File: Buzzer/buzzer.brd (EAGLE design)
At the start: 100 x 80 mm, 27 parts

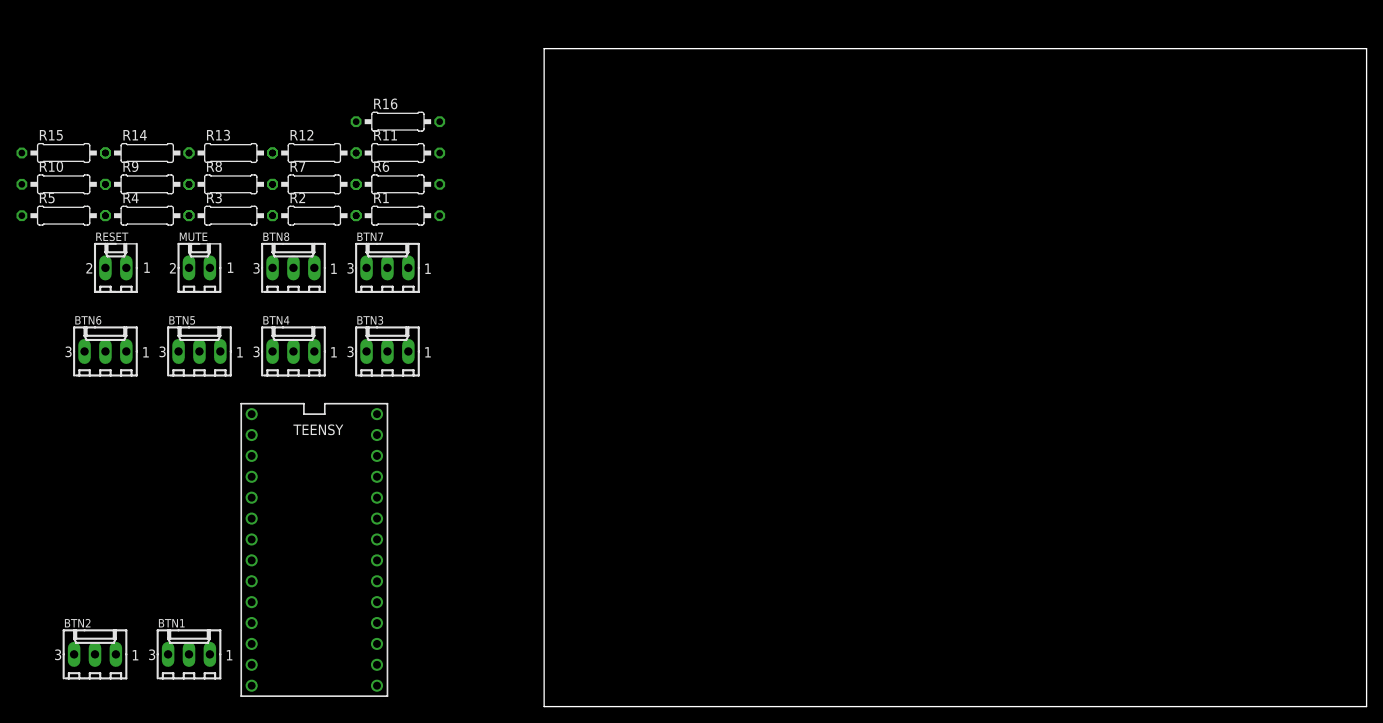
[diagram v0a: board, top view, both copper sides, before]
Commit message: Work on Eagle board design Unfinished, but it'll do as veroboard is a mess anyway
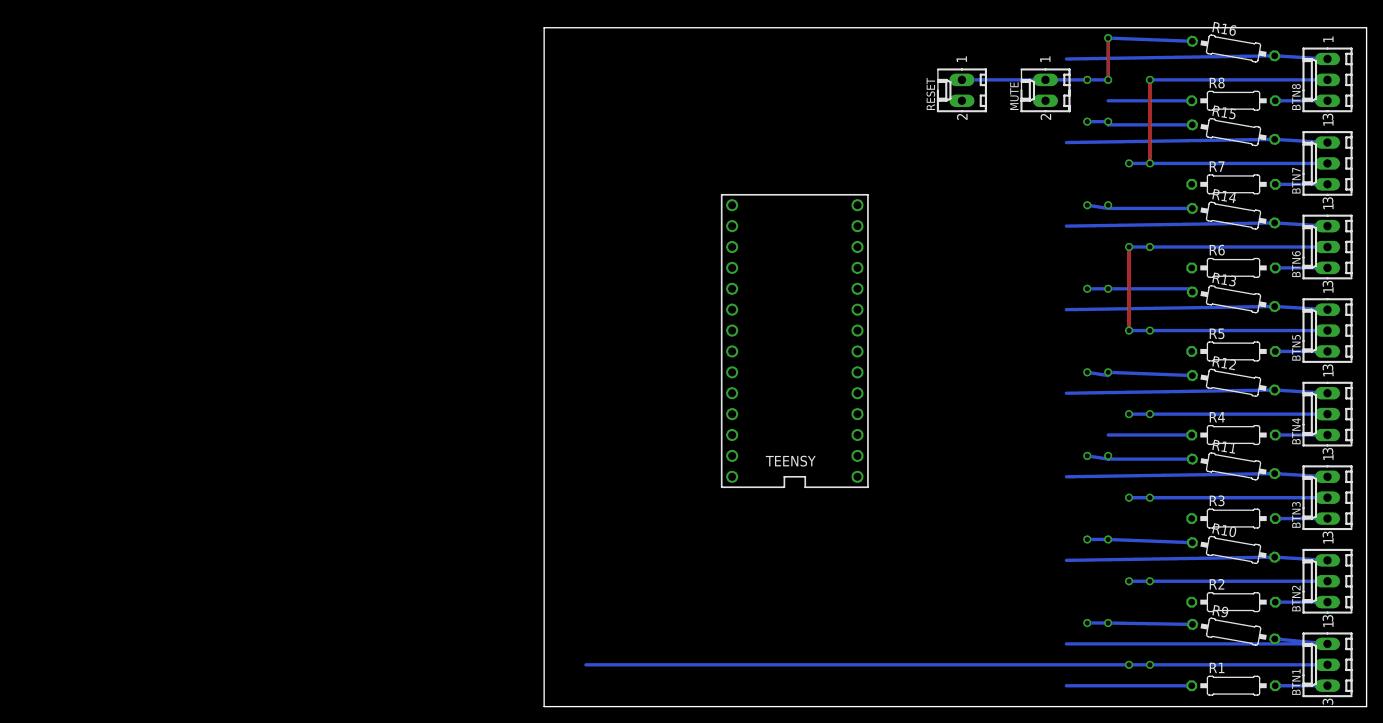
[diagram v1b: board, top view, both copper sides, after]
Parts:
- moved BTN2 150.1 mm to (95.2, 15.2), turned to 90 degrees
- moved BTN6 149.1 mm to (95.2, 55.9), turned to 90 degrees
- moved R10 149.0 mm to (83.8, 19.1), turned to 350 degrees
- moved R5 143.2 mm to (83.8, 43.2)
- moved R9 142.9 mm to (83.8, 9.11), turned to 350 degrees
- moved R15 142.3 mm to (83.8, 69.8), turned to 350 degrees
- moved BTN1 138.4 mm to (95.2, 5.08), turned to 90 degrees
- moved BTN5 137.2 mm to (95.2, 45.7), turned to 90 degrees
- moved R4 134.7 mm to (83.8, 33.0)
- moved R14 132.3 mm to (83.8, 59.7), turned to 350 degrees
- moved BTN8 127.8 mm to (95.2, 76.2), turned to 90 degrees
- moved R3 127.4 mm to (83.8, 22.9)
- moved BTN4 126.0 mm to (95.2, 35.6), turned to 90 degrees
- moved R13 123.2 mm to (83.8, 49.5), turned to 350 degrees
- moved R8 122.3 mm to (83.8, 73.7)
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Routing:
- net 5V: track 0.00 -> 276.9 mm, vias 0 -> 11
- net GND: track 0.00 -> 125.1 mm, vias 0 -> 8
- net IN1: track 0.00 -> 38.2 mm
- net IN8: track 0.00 -> 31.8 mm
- net IN7: track 0.00 -> 31.8 mm
- net IN6: track 0.00 -> 31.8 mm
- net IN5: track 0.00 -> 31.8 mm
- net IN4: track 0.00 -> 31.8 mm
- net IN3: track 0.00 -> 31.8 mm
- net IN2: track 0.00 -> 31.8 mm
- net LED1: track 0.00 -> 15.2 mm
- net LED8: track 0.00 -> 10.2 mm
- net LED4: track 0.00 -> 10.2 mm
- net N$9: track 0.00 -> 6.35 mm
- net N$6: track 0.00 -> 6.35 mm
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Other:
- board size 100 x 80 mm -> 100 x 82.5 mm
